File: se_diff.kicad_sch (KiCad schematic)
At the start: 12 parts

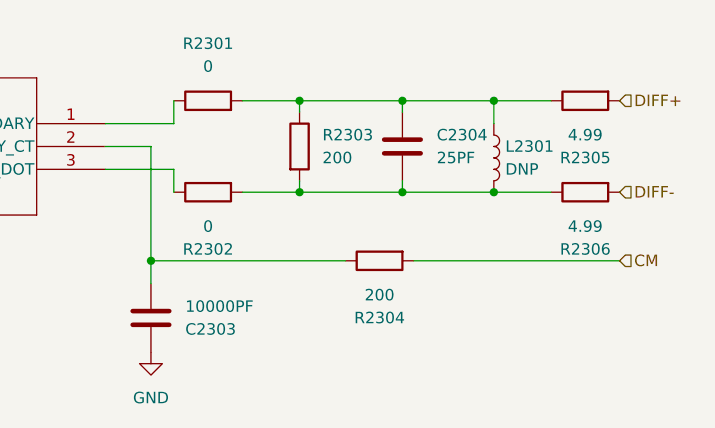
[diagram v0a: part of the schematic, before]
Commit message: Schematic Changes
Added Manufacturer/MPN/Description Fields to parts
Added libraries to project
Modified FMC schematic to use new symbol
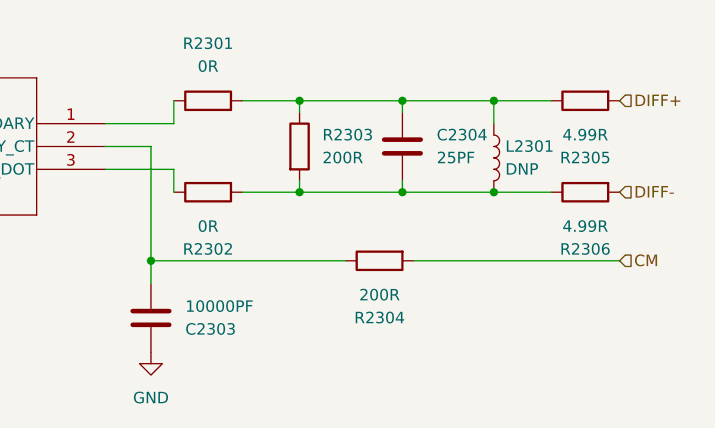
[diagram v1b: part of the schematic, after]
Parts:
- C2301, C2302, C2303: Manufacturer (none) -> TDK; Manufacturer Part Number (none) -> C1608C0G1E103J080AA
- C2304: Manufacturer (none) -> Samsung; Manufacturer Part Number (none) -> CL10C250JB8NNNC
- R2301, R2302: value 0 -> 0R; Manufacturer (none) -> Panasonic; Manufacturer Part Number (none) -> ERJ-3GEY0R00V
- R2303, R2304: value 200 -> 200R; Manufacturer (none) -> Susumu; Manufacturer Part Number (none) -> RR0816P-201-D
- R2305, R2306: value 4.99 -> 4.99R; Manufacturer (none) -> YAGEO; Manufacturer Part Number (none) -> RC0603FR-074R99L
- XMER2301: Manufacturer (none) -> Mini-Circuits; Manufacturer Part Number (none) -> TCM4-19+

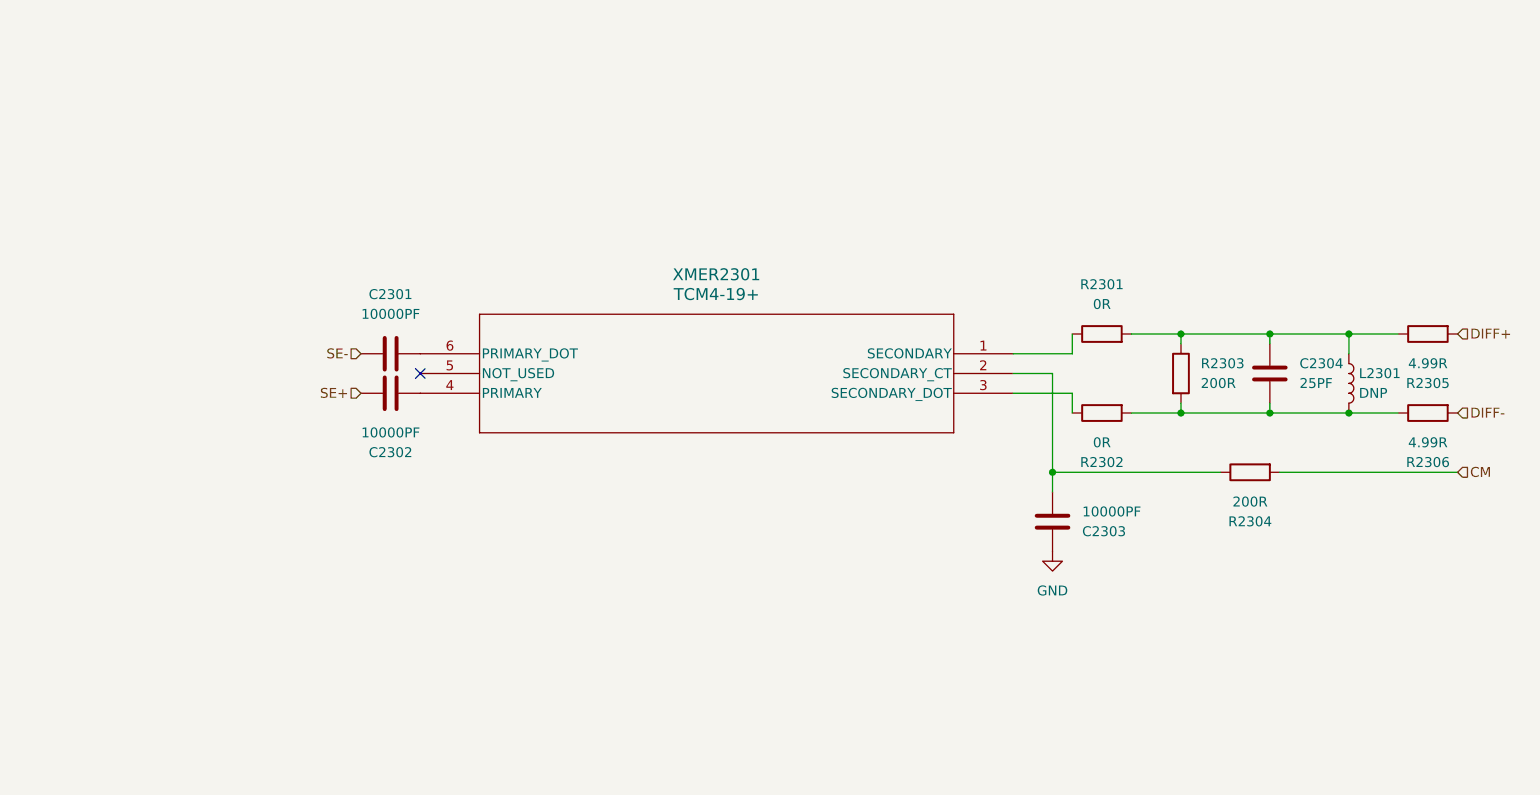
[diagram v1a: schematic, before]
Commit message: Schematics update
Cleaned up RF ADC and front end sections.
Verified that changes did not changes anything about the layout.
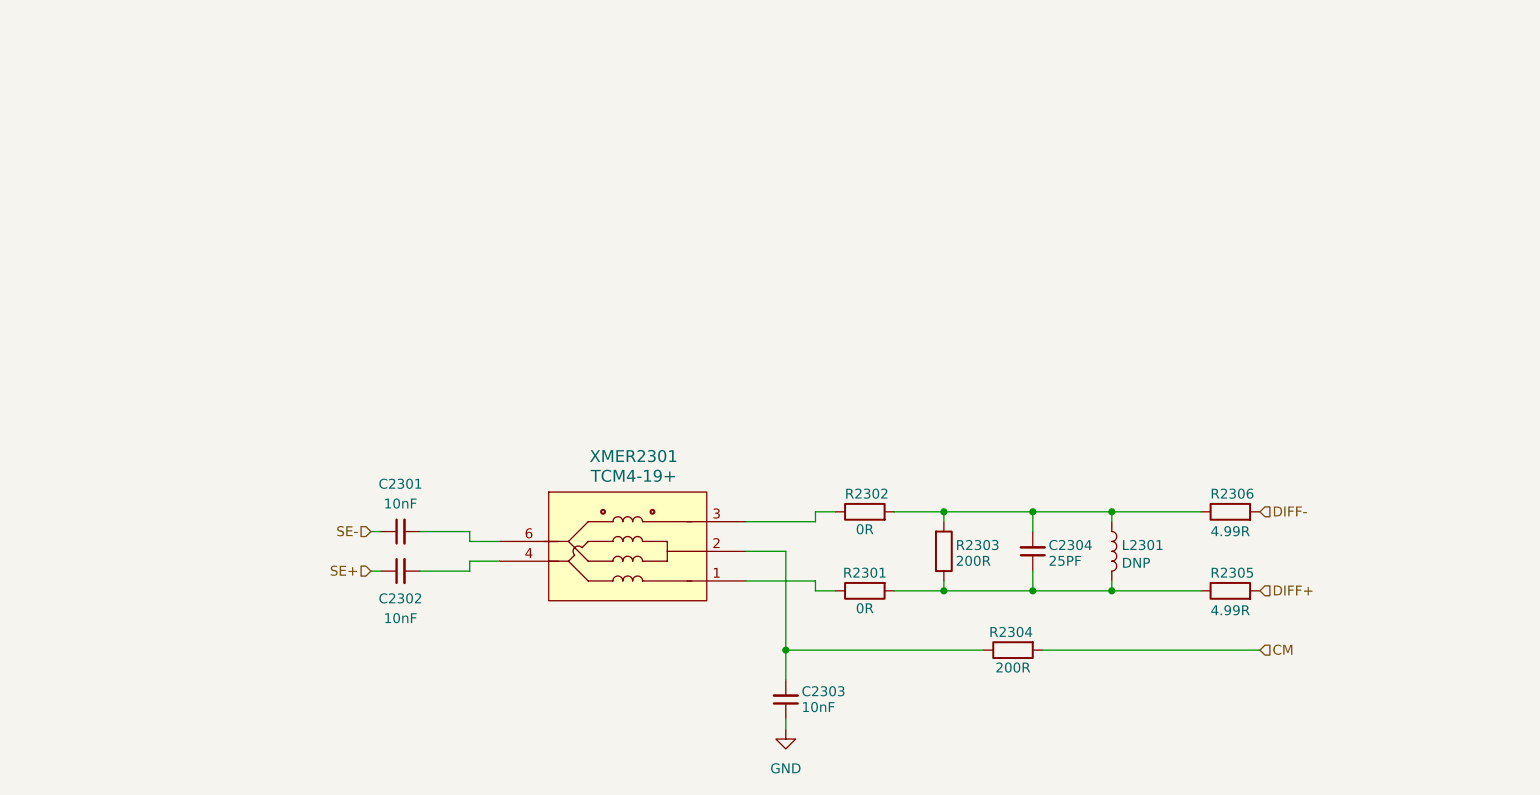
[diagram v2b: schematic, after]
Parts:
- C2301, C2302, C2303: value 10000PF -> 10nF; symbol Device:C -> Device:C_Small
- C2304: symbol Device:C -> Device:C_Small
- XMER2301: symbol 001_symbol:TCM4-19+ -> Zest_Custom:TCM4-19+
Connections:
- no-connect marks 1 -> 0
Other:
- moved on the sheet: C2301, C2302, C2303, C2304, L2301, R2301, R2302, R2303, R2304, R2305, R2306

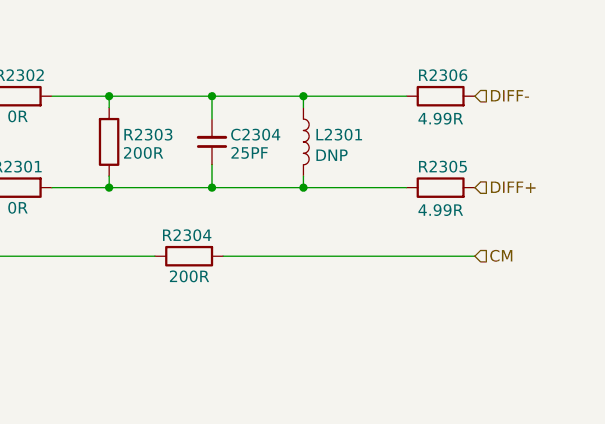
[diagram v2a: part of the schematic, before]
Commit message: Updated some Schematics
- updated slowmon schematic
- updated diff to se schematic
- cleaned up DRC/ERC errors
No changes were made that effected the PCB layout
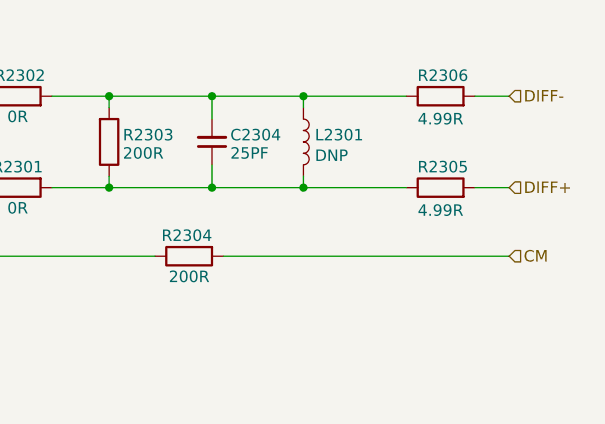
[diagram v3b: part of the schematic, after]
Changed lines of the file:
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@@
+	(wire
+		(pts
+			(xy 209.55 96.52) (xy 205.74 96.52)
+		)
+		(stroke
+			(width 0)
+			(type default)
+		)
+	)
 	(wire
 		(pts
@@
 	(wire
 		(pts
-			(xy 177.8 114.3) (xy 205.74 114.3)
+			(xy 209.55 106.68) (xy 205.74 106.68)
+		)
+		(stroke
+			(width 0)
+			(type default)
+		)
+	)
+	(wire
+		(pts
+			(xy 177.8 114.3) (xy 209.55 114.3)
 		)
 		(stroke
@@
 	(hierarchical_label "DIFF-"
 		(shape input)
-		(at 205.74 96.52 0)
+		(at 209.55 96.52 0)
 		(fields_autoplaced yes)
 		(effects
@@
 	(hierarchical_label "CM"
 		(shape input)
-		(at 205.74 114.3 0)
+		(at 209.55 114.3 0)
 		(fields_autoplaced yes)
 		(effects
@@
 	(hierarchical_label "DIFF+"
 		(shape input)
-		(at 205.74 106.68 0)
-		(fields_autoplaced yes)
-		(effects
+		(at 209.55 106.68 0)
+		(fields_autoplaced yes)
+		(effects

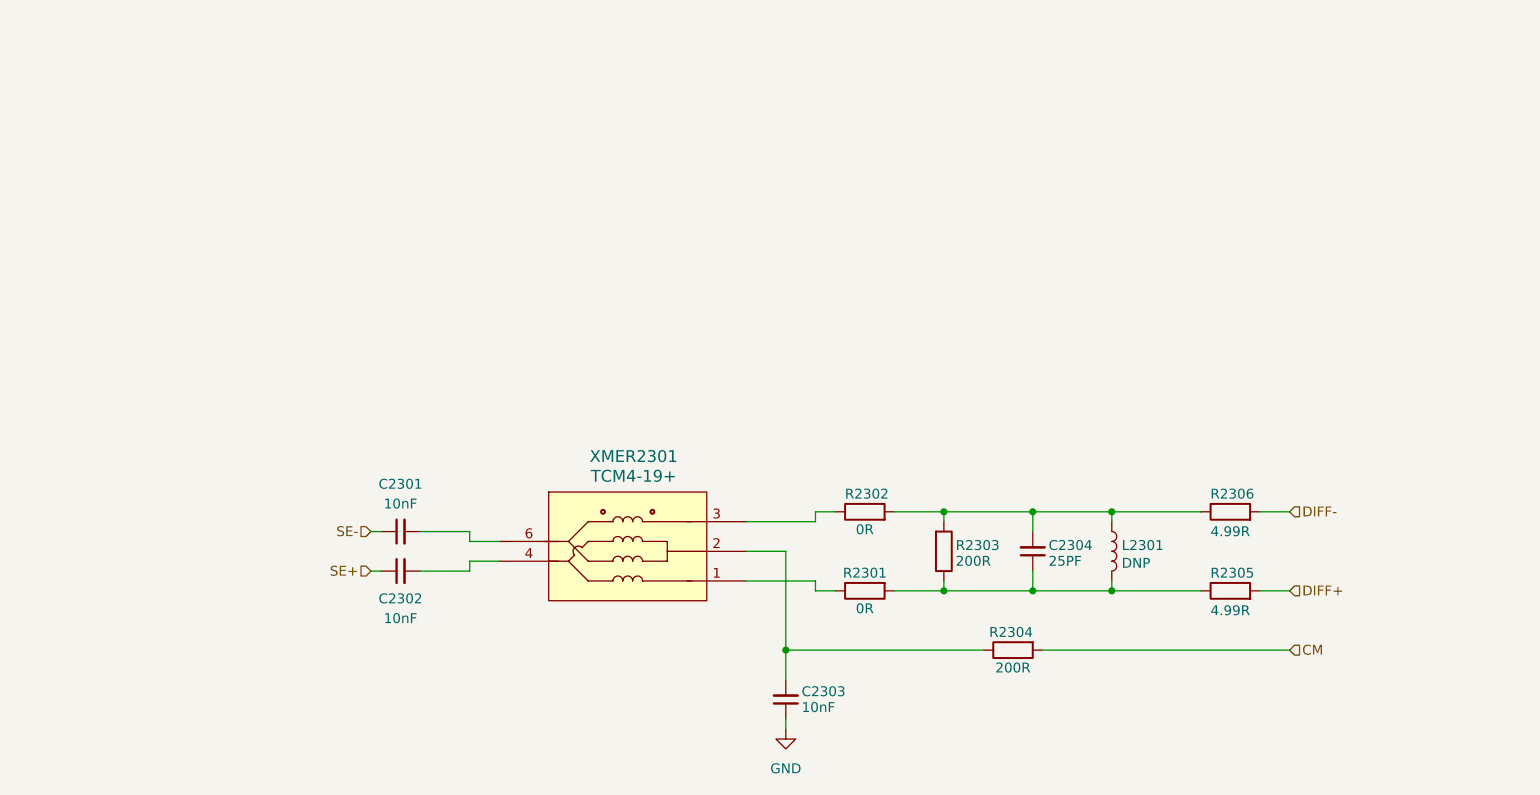
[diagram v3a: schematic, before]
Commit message: Made MPEX Changes
- Minimal Changes from main branch
- Changed ADC input section TCM4-19+ to TC1-1+
- Changed DAC output section TCM4-19+ to TC4-6T+
- Changed Silkscreen text to read MPEX Zest
- Added Documentation folder with pdfs of schematics and pcb prints
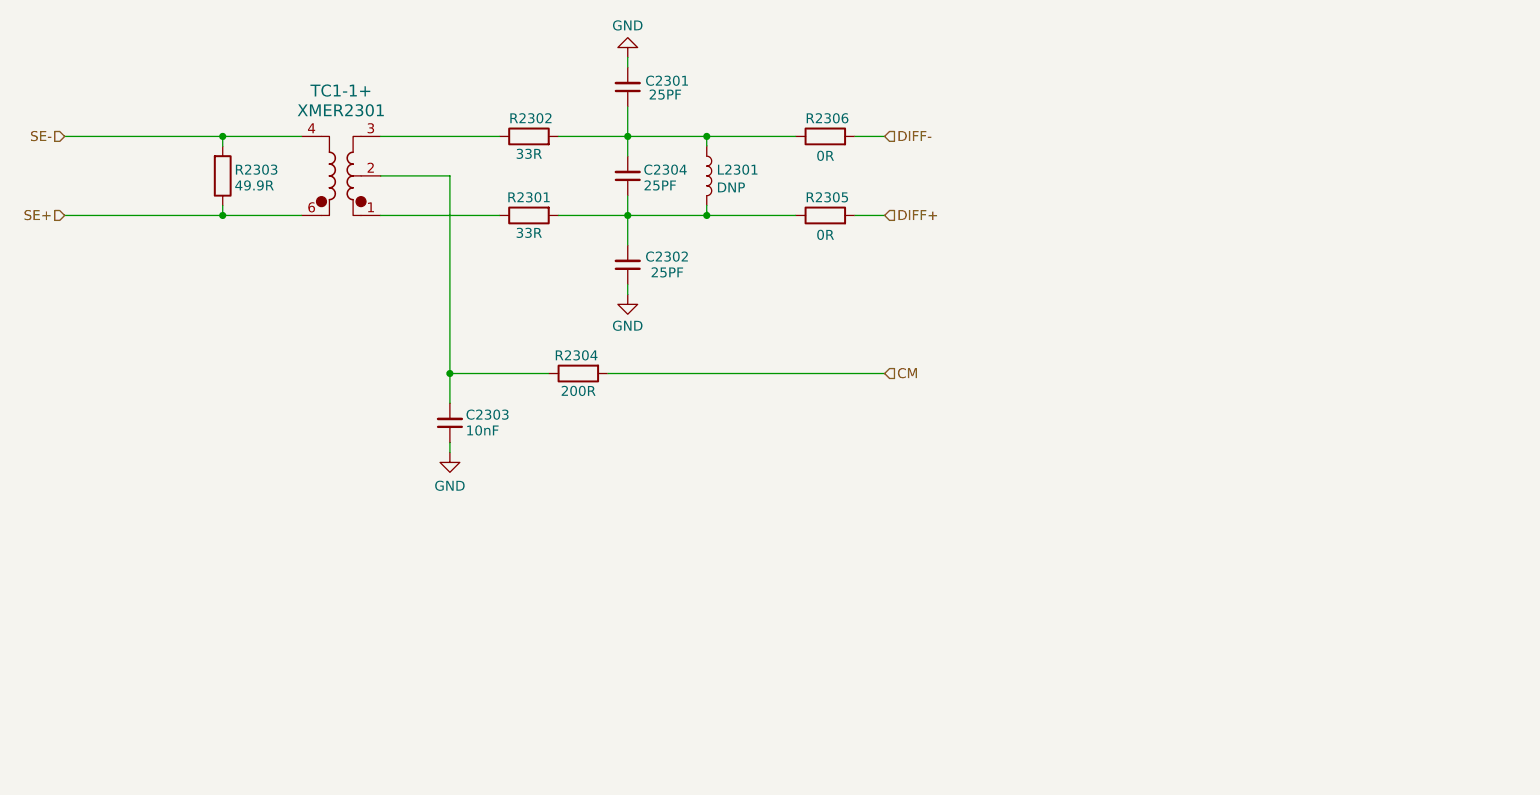
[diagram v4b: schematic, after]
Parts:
- C2301, C2302: value 10nF -> 25PF
- R2301, R2302: value 0R -> 33R
- R2303: value 200R -> 49.9R
- R2305, R2306: value 4.99R -> 0R
- XMER2301: value TCM4-19+ -> TC1-1+; footprint 001_download:DB714_MNC -> Transformer_SMD:Transformer_MiniCircuits_AT224-1A; symbol Zest_Custom:TCM4-19+ -> Zest_Custom:TC4-6; Manufacturer Part Number TCM4-19+ -> TC1-1+; Vendor digikey:TCM4-19+ -> digikey:3157-TC1-1+CT-ND
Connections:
- net GND: now also C2301.2, C2302.1
- net SE+: now also R2303.1, XMER2301.6; no longer C2302.1
- net SE-: now also R2303.2, XMER2301.4; no longer C2301.1
- net at C2304.2, L2301.2, R2302.2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: now also C2301.1; no longer R2303.2
- net at C2304.1, L2301.1, R2301.2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: now also C2302.2; no longer R2303.1
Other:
- moved on the sheet: C2301, C2302, C2303, C2304, L2301, R2301, R2302, R2303, R2304, R2305, R2306

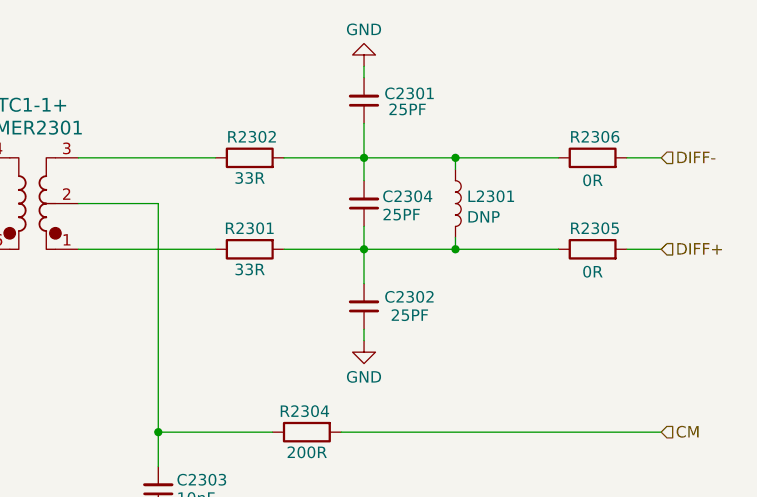
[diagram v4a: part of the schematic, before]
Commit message: Further Project cleanup
-Added BOM and fabrication files
-updated all documentation files
- Added suggested DC blocking cap at DAC outputs

-Set DRC to 5mil trace and space and fixed various violations detailed below
- Removed various small tracks overlapping IC pads on U2701,U2901,U3101,U3201
- Spaced vias 5 mil apart around U701, U201, 1201
- Moved LMK_CLKout3 pair on In4 layer away from PMOD1_1 pin
- adjusted track into pin47 on U701 to clear pin 48
- adjusted trace under U903 to give more room from ground pads/vias
- spaced out vias around pins45/46 of U201

-Many tweak to trace to go through the center of pad throughout the design
-An example is the trace around C3005
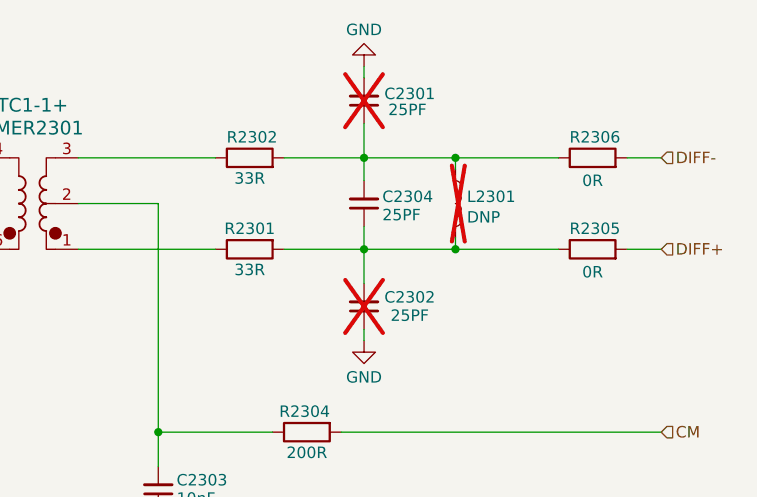
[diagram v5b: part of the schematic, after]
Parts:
- C2301, C2302, L2301: now not fitted
- R2301, R2302: Manufacturer Panasonic -> Susumu; Manufacturer Part Number ERJ-3GEY0R00V -> RR0816Q-330-D; Vendor digikey:P0.0GCT-ND -> digikey:RR08Q33DCT-ND
- R2303: Manufacturer Susumu -> Vishay Dale; Manufacturer Part Number RR0816P-201-D -> TNPW060349R9BEEA; Vendor digikey:RR08P200DCT-ND -> digikey:541-2031-1-ND
- R2305, R2306: Manufacturer YAGEO -> Panasonic; Manufacturer Part Number RC0603FR-074R99L -> ERJ-3GEY0R00V; Vendor digikey:311-4.99HRCT-ND -> digikey:P0.0GCT-ND
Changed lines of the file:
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@@
 			)
 		)
-		(property "Description" "RES 4.99 OHM 1% 1/10W 0603"
+		(property "Description" "RES SMD 0 OHM JUMPER 1/10W 0603"
 			(at 149.86 48.26 0)
 			(effects
@@
 			)
 		)
-		(property "Vendor" "digikey:311-4.99HRCT-ND"
+		(property "Vendor" "digikey:P0.0GCT-ND"
 			(at 233.68 275.59 0)
 			(effects
@@
 			)
 		)
-		(property "Manufacturer" "YAGEO "
+		(property "Manufacturer" "Panasonic"
 			(at 149.86 48.26 0)
 			(effects
@@
 			)
 		)
-		(property "Manufacturer Part Number" "RC0603FR-074R99L "
+		(property "Manufacturer Part Number" "ERJ-3GEY0R00V "
 			(at 149.86 48.26 0)
 			(effects
@@
 		(in_bom yes)
 		(on_board yes)
-		(dnp no)
+		(dnp yes)
 		(property "Reference" "L2301"
 			(at 135.89 52.5781 0)
@@
 		(in_bom yes)
 		(on_board yes)
-		(dnp no)
+		(dnp yes)
 		(property "Reference" "C2302"
 			(at 129.54 63.754 0)
@@
 		(in_bom yes)
 		(on_board yes)
-		(dnp no)
+		(dnp yes)
 		(property "Reference" "C2301"
 			(at 129.54 41.148 0)
@@
 			)
 		)
-		(property "Description" "RES SMD 200 OHM 0.5% 1/16W 0603"
+		(property "Description" "RES 49.9 OHM 0.1% 0.21W 0603"
 			(at 72.39 53.34 0)
 			(effects
@@
 			)
 		)
-		(property "Vendor" "digikey:RR08P200DCT-ND"
+		(property "Vendor" "digikey:541-2031-1-ND"
 			(at -123.19 -25.4 0)
 			(effects
@@
 			)
 		)
-		(property "Manufacturer" "Susumu "
+		(property "Manufacturer" "Vishay Dale"
 			(at 72.39 53.34 0)
 			(effects
@@
 			)
 		)
-		(property "Manufacturer Part Number" "RR0816P-201-D "
+		(property "Manufacturer Part Number" "TNPW060349R9BEEA"
 			(at 72.39 53.34 0)
 			(effects
@@
 			)
 		)
-		(property "Description" "RES SMD 0 OHM JUMPER 1/10W 0603"
+		(property "Description" "RES SMD 33 OHM 0.5% 1/16W 0603"
 			(at 111.76 58.42 0)
 			(effects
@@
 			)
 		)
-		(property "Vendor" "digikey:P0.0GCT-ND"
+		(property "Vendor" "digikey:RR08Q33DCT-ND"
 			(at 185.42 -127 0)
 			(effects
@@
 			)
 		)
-		(property "Manufacturer" "Panasonic"
+		(property "Manufacturer" "Susumu"
 			(at 111.76 58.42 0)
 			(effects
@@
 			)
 		)
-		(property "Manufacturer Part Number" "ERJ-3GEY0R00V "
+		(property "Manufacturer Part Number" "RR0816Q-330-D"
 			(at 111.76 58.42 0)
 			(effects
@@
 			)
 		)
-		(property "Description" "RES SMD 0 OHM JUMPER 1/10W 0603"
+		(property "Description" "RES SMD 33 OHM 0.5% 1/16W 0603"
 			(at 111.76 48.26 0)
 			(effects
@@
 			)
 		)
-		(property "Vendor" "digikey:P0.0GCT-ND"
+		(property "Vendor" "digikey:RR08Q33DCT-ND"
 			(at 195.58 233.68 0)
 			(effects
@@
 			)
 		)
-		(property "Manufacturer" "Panasonic"
+		(property "Manufacturer" "Susumu"
 			(at 111.76 48.26 0)
 			(effects
@@
 			)
 		)
-		(property "Manufacturer Part Number" "ERJ-3GEY0R00V "
+		(property "Manufacturer Part Number" "RR0816Q-330-D"
 			(at 111.76 48.26 0)
 			(effects
@@
 			)
 		)
-		(property "Description" "CAP CER 10nF 25V C0G 0603"
+		(property "Description" "CAP CER 10000PF 25V C0G 0603"
 			(at 101.6 85.09 0)
 			(effects
@@
 			)
 		)
-		(property "Description" "RES 4.99 OHM 1% 1/10W 0603"
+		(property "Description" "RES SMD 0 OHM JUMPER 1/10W 0603"
 			(at 149.86 58.42 0)
 			(effects
@@
 			)
 		)
-		(property "Vendor" "digikey:311-4.99HRCT-ND"
+		(property "Vendor" "digikey:P0.0GCT-ND"
 			(at 223.52 285.75 0)
 			(effects
@@
 			)
 		)
-		(property "Manufacturer" "YAGEO "
+		(property "Manufacturer" "Panasonic"
 			(at 149.86 58.42 0)
 			(effects
@@
 			)
 		)
-		(property "Manufacturer Part Number" "RC0603FR-074R99L "
+		(property "Manufacturer Part Number" "ERJ-3GEY0R00V "
 			(at 149.86 58.42 0)
 			(effects
